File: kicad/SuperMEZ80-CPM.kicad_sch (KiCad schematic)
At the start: 17 parts, among them J1 EMUZ80_0, J2 EMUZ80, J4 ext SPI, U1 Z80CPU, U2 AS6C4008, U3 MCP23S08-xP

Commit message: Add first version of SuperMEZ80-CPM PCB
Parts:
- removed JP1, JP2: Jumper_2_Open, Jumper:SolderJumper-2_P1.3mm_Open_TrianglePad1.0x1.5mm, symbol Jumper:Jumper_2_Open
- removed R4: 10K, Resistor_SMD:R_0603_1608Metric_Pad0.98x0.95mm_HandSolder, symbol Device:R
- removed U3: MCP23S08-xP, Package_DIP:DIP-18_W7.62mm, symbol library:MCP23S08-xP
- added C5, C6, C7, C8: 100nF, Capacitor_SMD:C_0603_1608Metric_Pad1.08x0.95mm_HandSolder, symbol Device:C
- added D2: M1, LED_THT:LED_D1.8mm_W3.3mm_H2.4mm, symbol Device:LED
- added D3: POWER, LED_THT:LED_D1.8mm_W3.3mm_H2.4mm, symbol Device:LED
- added J3: Conn_02x03_Odd_Even, Connector_PinHeader_2.54mm:PinHeader_2x03_P2.54mm_Vertical, symbol Connector_Generic:Conn_02x03_Odd_Even
- added J4: Conn_02x01, Connector_PinHeader_2.54mm:PinHeader_1x02_P2.54mm_Vertical, symbol Connector_Generic:Conn_02x01
- added J5: Conn_02x02_Odd_Even, Connector_PinHeader_2.54mm:PinHeader_2x02_P2.54mm_Vertical, symbol Connector_Generic:Conn_02x02_Odd_Even
- added J7: SD Card slot, Connector_PinHeader_2.54mm:PinHeader_1x06_P2.54mm_Vertical, symbol Connector:Conn_01x06_Socket
- added R1, R2: 100, Resistor_THT:R_Axial_DIN0204_L3.6mm_D1.6mm_P7.62mm_Horizontal, symbol Device:R
- added R10, R11, R12, R13, R14, R8, R9: 10K, Resistor_SMD:R_0603_1608Metric_Pad0.98x0.95mm_HandSolder, symbol Device:R
- added R5, R6: 100, Resistor_SMD:R_0603_1608Metric_Pad0.98x0.95mm_HandSolder, symbol Device:R
- added RN1: 10K, Resistor_THT:R_Array_SIP9, symbol Device:R_Network08_US
- C3, C4: footprint Capacitor_SMD:C_0603_1608Metric_Pad1.08x0.95mm_HandSolder -> Capacitor_THT:C_Disc_D4.3mm_W1.9mm_P5.00mm
- D1: value LED -> DISK
- J6: renamed from J4; value ext SPI -> SD Card slot
- R3: value 10K -> 100; footprint Resistor_SMD:R_0603_1608Metric_Pad0.98x0.95mm_HandSolder -> Resistor_THT:R_Axial_DIN0204_L3.6mm_D1.6mm_P7.62mm_Horizontal
- R4: renamed from R2; value 1.5K -> 100; footprint Resistor_THT:R_Axial_DIN0204_L3.6mm_D1.6mm_P7.62mm_Horizontal -> Resistor_SMD:R_0603_1608Metric_Pad0.98x0.95mm_HandSolder
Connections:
- net A18 is gone; now on net GND: U2.1 (A18)
- net ~{CS1} is gone; now on net ~{SS}: J6.1 (~{CS})
- net ~{CS} is gone; now on net ~{NMI}: J1.16 (RE2)
- net ~{RD} is gone; now on net ~{OE}: J2.20 (RA5), U1.21 (~{RD})
- net +5V: now also J2.16 (VCC), R3.1, C5.1, C6.1, C7.1, C8.1, J5.1 (Pin_1), J5.2 (Pin_2), J7.5 (VCC), R1.1, R2.1, R5.1, R6.1; no longer R7.1
- net A10: now also R14.1, RN1.9 (R8); no longer J2.1
- net A11: now also R13.1, RN1.8 (R7); no longer J1.1
- net A12: now also R9.1, RN1.4 (R3); no longer J1.2
- net A13: now also R10.1, RN1.5 (R4); no longer J1.3
- net A14: now also J1.4 (RD6), R8.1, RN1.3 (R2); no longer R3.1
- net A15: now also J1.5 (RD7), R7.1, RN1.2 (R1)
- net A16: now also J3.2 (Pin_2)
- net A17: now also J3.4 (Pin_4)
- net A8: now also R11.1, RN1.6 (R5); no longer J2.3
- net A9: now also R12.1, RN1.7 (R6); no longer J2.2
- net BANK0: now also J1.2 (RD4), J3.1 (Pin_1)
- net BANK1: now also J1.3 (RD5), J3.3 (Pin_3)
- net CLK: now also J4.2 (Pin_2); no longer J1.6 (RA3)
- net D0: no longer J6.3 (MOSI)
- net D1: no longer J6.2 (SCK)
- net GND: now also R7.2, C5.2, C6.2, C7.2, C8.2, D3.1 (K), J5.3 (Pin_3), J5.4 (Pin_4), J7.6 (GND), R10.2, R11.2, R12.2, R13.2, R14.2, R8.2, R9.2, RN1.1 (common); no longer R3.2, U2.22 (~{CE})
- net MISO: now also J1.1 (RD3), J7.4 (MISO)
- net ~{BUSRQ}: now also J2.13 (RA2); no longer J2.19 (RE0)
- net ~{NMI}: no longer R7.2
- net ~{OE}: no longer J2.17 (RA4)
- net ~{WAIT}: now also J2.17 (RA4); no longer J1.5 (RD7)
- net ~{WE}: now also J2.19 (RE0), U1.22 (~{WR}); no longer J2.13 (RA2)
- net at D1.2 (A), R4.2: now also R1.2
- net ~{M1}: now reaches U1.27 (~{M1})
- net ~{M1}: now also D2.1 (K)
- net ~{CS0} renamed ~{SS}
- net ~{SS}: now also J2.3 (RD0), J7.1 (~{CS})
- net ~{MREQ} renamed ~{CE}
- net ~{CE}: now also U2.22 (~{CE})
- net ~{RFSH}: no longer names the net of U1.28 (~{RFSH})
- net ~{RFSH}: no longer J1.4 (RD6)
- new net: D3.2 (A), R3.2, R6.2
- new net: D2.2 (A), R2.2, R5.2
- new net MOSI: J2.2 (RD1), J6.3 (MOSI), J7.3 (MOSI)
- new net RA3: J1.6 (RA3), J4.1 (Pin_1)
- new net SCK: J2.1 (RD2), J6.2 (SCK), J7.2 (SCK)
- no-connect marks 10 -> 9
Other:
- removed sheet Untitled Sheet
- note removed: "optional pull-up/down resisters and jumpers"
- title: SuperMEZ80+SPI -> SuperMEZ80-CPM
- moved on the sheet: C1, C2, D1, J6, R4

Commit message: Add SuperMEZ80-CPM version 1.0
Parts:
- removed C2, C3: 100nF, Capacitor_THT:C_Disc_D4.3mm_W1.9mm_P5.00mm, symbol Device:C
- removed C6, C7: 100nF, Capacitor_SMD:C_0603_1608Metric_Pad1.08x0.95mm_HandSolder, symbol Device:C
- removed J3: Conn_02x03_Odd_Even, Connector_PinHeader_2.54mm:PinHeader_2x03_P2.54mm_Vertical, symbol Connector_Generic:Conn_02x03_Odd_Even
- removed J5: Conn_02x02_Odd_Even, Connector_PinHeader_2.54mm:PinHeader_2x02_P2.54mm_Vertical, symbol Connector_Generic:Conn_02x02_Odd_Even
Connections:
- net BANK0 is gone; now on net A16: J1.2 (RD4)
- net BANK1 is gone; now on net A17: J1.3 (RD5)
- no-connect marks 9 -> 7

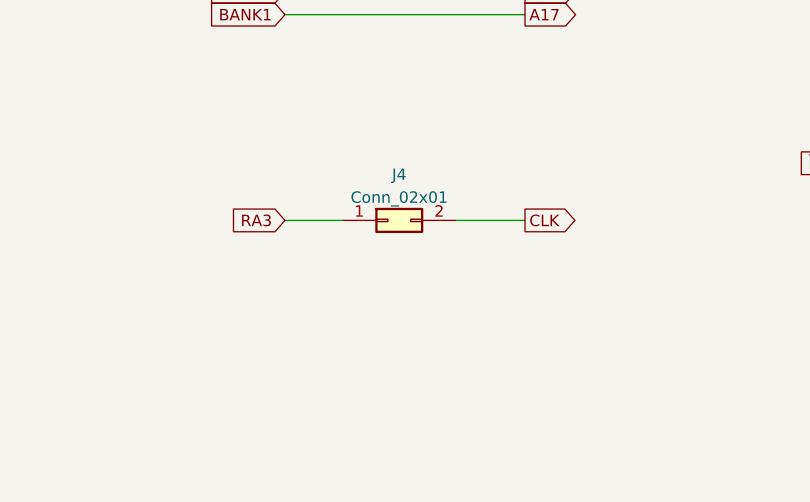
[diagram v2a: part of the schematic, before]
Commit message: Add SuperMEZ80-CPM version 1.1 and update README.md
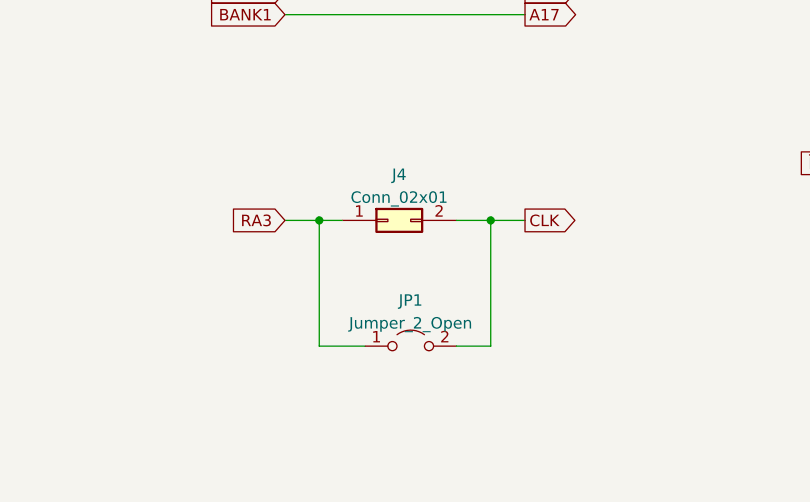
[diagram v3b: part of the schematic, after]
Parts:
- added JP1: Jumper_2_Open, Jumper:SolderJumper-2_P1.3mm_Open_TrianglePad1.0x1.5mm, symbol Jumper:Jumper_2_Open
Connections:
- net CLK: now also JP1.2 (B)
- net RA3: now also JP1.1 (A)
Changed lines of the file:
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@@
   (title_block
     (title "SuperMEZ80-CPM")
-    (date "2023-07-17")
-    (rev "1.0")
+    (date "2023-08-25")
+    (rev "1.1")
   )
   (junction (at 260.35 40.64) (diameter 0) (color 0 0 0 0)
@@
   (junction (at 91.44 127) (diameter 0) (color 0 0 0 0)
   )
+  (junction (at 135.89 160.02) (diameter 0) (color 0 0 0 0)
+  )
   (junction (at 260.35 45.72) (diameter 0) (color 0 0 0 0)
   )
@@
   )
   (junction (at 115.57 20.32) (diameter 0) (color 0 0 0 0)
+  )
+  (junction (at 154.94 160.02) (diameter 0) (color 0 0 0 0)
   )
   (junction (at 260.35 38.1) (diameter 0) (color 0 0 0 0)
@@
     (stroke (width 0) (type default))
   )
+  (wire (pts (xy 135.89 160.02) (xy 138.43 160.02))
+    (stroke (width 0) (type default))
+  )
   (wire (pts (xy 260.35 134.62) (xy 255.27 134.62))
     (stroke (width 0) (type default))
@@
     (stroke (width 0) (type default))
   )
+  (wire (pts (xy 135.89 173.99) (xy 135.89 160.02))
+    (stroke (width 0) (type default))
+  )
   (bus (pts (xy 91.44 44.45) (xy 91.44 41.91))
     (stroke (width 0) (type default))
@@
     (stroke (width 0) (type default))
   )
-  (wire (pts (xy 158.75 160.02) (xy 151.13 160.02))
+  (wire (pts (xy 158.75 160.02) (xy 154.94 160.02))
     (stroke (width 0) (type default))
   )
@@
     (stroke (width 0) (type default))
   )
+  (wire (pts (xy 154.94 173.99) (xy 154.94 160.02))
+    (stroke (width 0) (type default))
+  )
   (wire (pts (xy 77.47 134.62) (xy 88.9 134.62))
     (stroke (width 0) (type default))
@@
     (stroke (width 0) (type default))
   )
+  (wire (pts (xy 151.13 173.99) (xy 154.94 173.99))
+    (stroke (width 0) (type default))
+  )
   (bus (pts (xy 115.57 85.09) (xy 115.57 105.41))
     (stroke (width 0) (type default))
@@
     (stroke (width 0) (type default))
   )
+  (wire (pts (xy 154.94 160.02) (xy 151.13 160.02))
+    (stroke (width 0) (type default))
+  )
   (bus (pts (xy 91.44 69.85) (xy 91.44 67.31))
     (stroke (width 0) (type default))
@@
     (stroke (width 0) (type default))
   )
+  (wire (pts (xy 140.97 173.99) (xy 135.89 173.99))
+    (stroke (width 0) (type default))
+  )
   (wire (pts (xy 45.72 154.94) (xy 52.07 154.94))
     (stroke (width 0) (type default))
@@
     (stroke (width 0) (type default))
   )
-  (wire (pts (xy 132.08 160.02) (xy 138.43 160.02))
+  (wire (pts (xy 132.08 160.02) (xy 135.89 160.02))
     (stroke (width 0) (type default))
   )
@@
         )
       )
+    )
+  )
+  (symbol (lib_id "Jumper:Jumper_2_Open") (at 146.05 173.99 0) (unit 1)
+    (in_bom yes) (on_board yes) (dnp no)
+    (property "Reference" "JP1" (at 146.05 168.91 0)
+      (effects (font (size 1.27 1.27)))
+    )
+    (property "Value" "Jumper_2_Open" (at 146.05 171.45 0)
+      (effects (font (size 1.27 1.27)))
+    )
+    (property "Footprint" "Jumper:SolderJumper-2_P1.3mm_Open_TrianglePad1.0x1.5mm" (at 146.05 173.99 0)
+      (effects (font (size 1.27 1.27)) hide)
+    )
+    (property "Datasheet" "~" (at 146.05 173.99 0)
+      (effects (font (size 1.27 1.27)) hide)
+    )
+    (pin "1")
+    (pin "2")
+    (instances
+      (project "SuperMEZ80-CPM"
+        (path "/d0b67a06-521c-429c-b0a7-be22c54278d6"
+          (reference "JP1") (unit 1)
+        )
+      )

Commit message: Add SuperMEZ80-CPM version 1.2
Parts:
- added R15: 10K, Resistor_SMD:R_0603_1608Metric_Pad0.98x0.95mm_HandSolder, symbol Device:R
- JP1: footprint Jumper:SolderJumper-2_P1.3mm_Open_TrianglePad1.0x1.5mm -> Jumper:SolderJumper-2_P1.3mm_Open_RoundedPad1.0x1.5mm
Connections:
- net GND: now also R15.2
- net ~{RESET}: now also R15.1
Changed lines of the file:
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@@
   (title_block
     (title "SuperMEZ80-CPM")
-    (date "2023-08-25")
-    (rev "1.1")
+    (date "2023-09-19")
+    (rev "1.2")
   )
   (junction (at 260.35 40.64) (diameter 0) (color 0 0 0 0)
@@
   )
   (junction (at 260.35 53.34) (diameter 0) (color 0 0 0 0)
+  )
+  (junction (at 266.7 38.1) (diameter 0) (color 0 0 0 0)
   )
   (junction (at 260.35 50.8) (diameter 0) (color 0 0 0 0)
@@
     (stroke (width 0) (type default))
   )
+  (wire (pts (xy 266.7 26.67) (xy 266.7 38.1))
+    (stroke (width 0) (type default))
+  )
   (bus (pts (xy 91.44 105.41) (xy 91.44 127))
     (stroke (width 0) (type default))
@@
     (stroke (width 0) (type default))
   )
+  (wire (pts (xy 243.84 26.67) (xy 250.19 26.67))
+    (stroke (width 0) (type default))
+  )
   (wire (pts (xy 257.81 40.64) (xy 260.35 40.64))
     (stroke (width 0) (type default))
@@
   )
   (wire (pts (xy 198.12 55.88) (xy 207.01 55.88))
+    (stroke (width 0) (type default))
+  )
+  (wire (pts (xy 257.81 26.67) (xy 266.7 26.67))
     (stroke (width 0) (type default))
   )
@@
     (effects (font (size 1.27 1.27)) (justify right))
     (property "Intersheetrefs" "${INTERSHEET_REFS}" (at 129.1137 114.3 0)
+      (effects (font (size 1.27 1.27)) (justify right) hide)
+    )
+  )
+  (global_label "~{RESET}" (shape output) (at 243.84 26.67 180) (fields_autoplaced)
+    (effects (font (size 1.27 1.27)) (justify right))
+    (property "Intersheetrefs" "${INTERSHEET_REFS}" (at 235.1891 26.67 0)
       (effects (font (size 1.27 1.27)) (justify right) hide)
     )
@@
     )
   )
+  (symbol (lib_id "Device:R") (at 254 26.67 90) (unit 1)
+    (in_bom yes) (on_board yes) (dnp no)
+    (property "Reference" "R15" (at 248.92 25.4 90)
+      (effects (font (size 1.27 1.27)))
+    )
+    (property "Value" "10K" (at 254 26.67 90)
+      (effects (font (size 1.27 1.27)))
+    )
+    (property "Footprint" "Resistor_SMD:R_0603_1608Metric_Pad0.98x0.95mm_HandSolder" (at 254 28.448 90)
+      (effects (font (size 1.27 1.27)) hide)
+    )
+    (property "Datasheet" "~" (at 254 26.67 0)
+      (effects (font (size 1.27 1.27)) hide)
+    )
+    (pin "1")
+    (pin "2")
+    (instances
+      (project "SuperMEZ80-CPM"
+        (path "/d0b67a06-521c-429c-b0a7-be22c54278d6"
+          (reference "R15") (unit 1)
+        )
+      )
+    )
+  )
   (symbol (lib_id "Device:R") (at 254 55.88 90) (unit 1)
     (in_bom yes) (on_board yes) (dnp no)
@@
       (effects (font (size 1.27 1.27)))
     )
-    (property "Footprint" "Jumper:SolderJumper-2_P1.3mm_Open_TrianglePad1.0x1.5mm" (at 146.05 173.99 0)
-      (effects (font (size 1.27 1.27)) hide)
-    )
+    (property "Footprint" "Jumper:SolderJumper-2_P1.3mm_Open_RoundedPad1.0x1.5mm" (at 146.05 173.99 0)
+      (effects (font (size 1.27 1.27)) hide)
+    )
